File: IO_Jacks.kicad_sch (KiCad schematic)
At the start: 25 parts

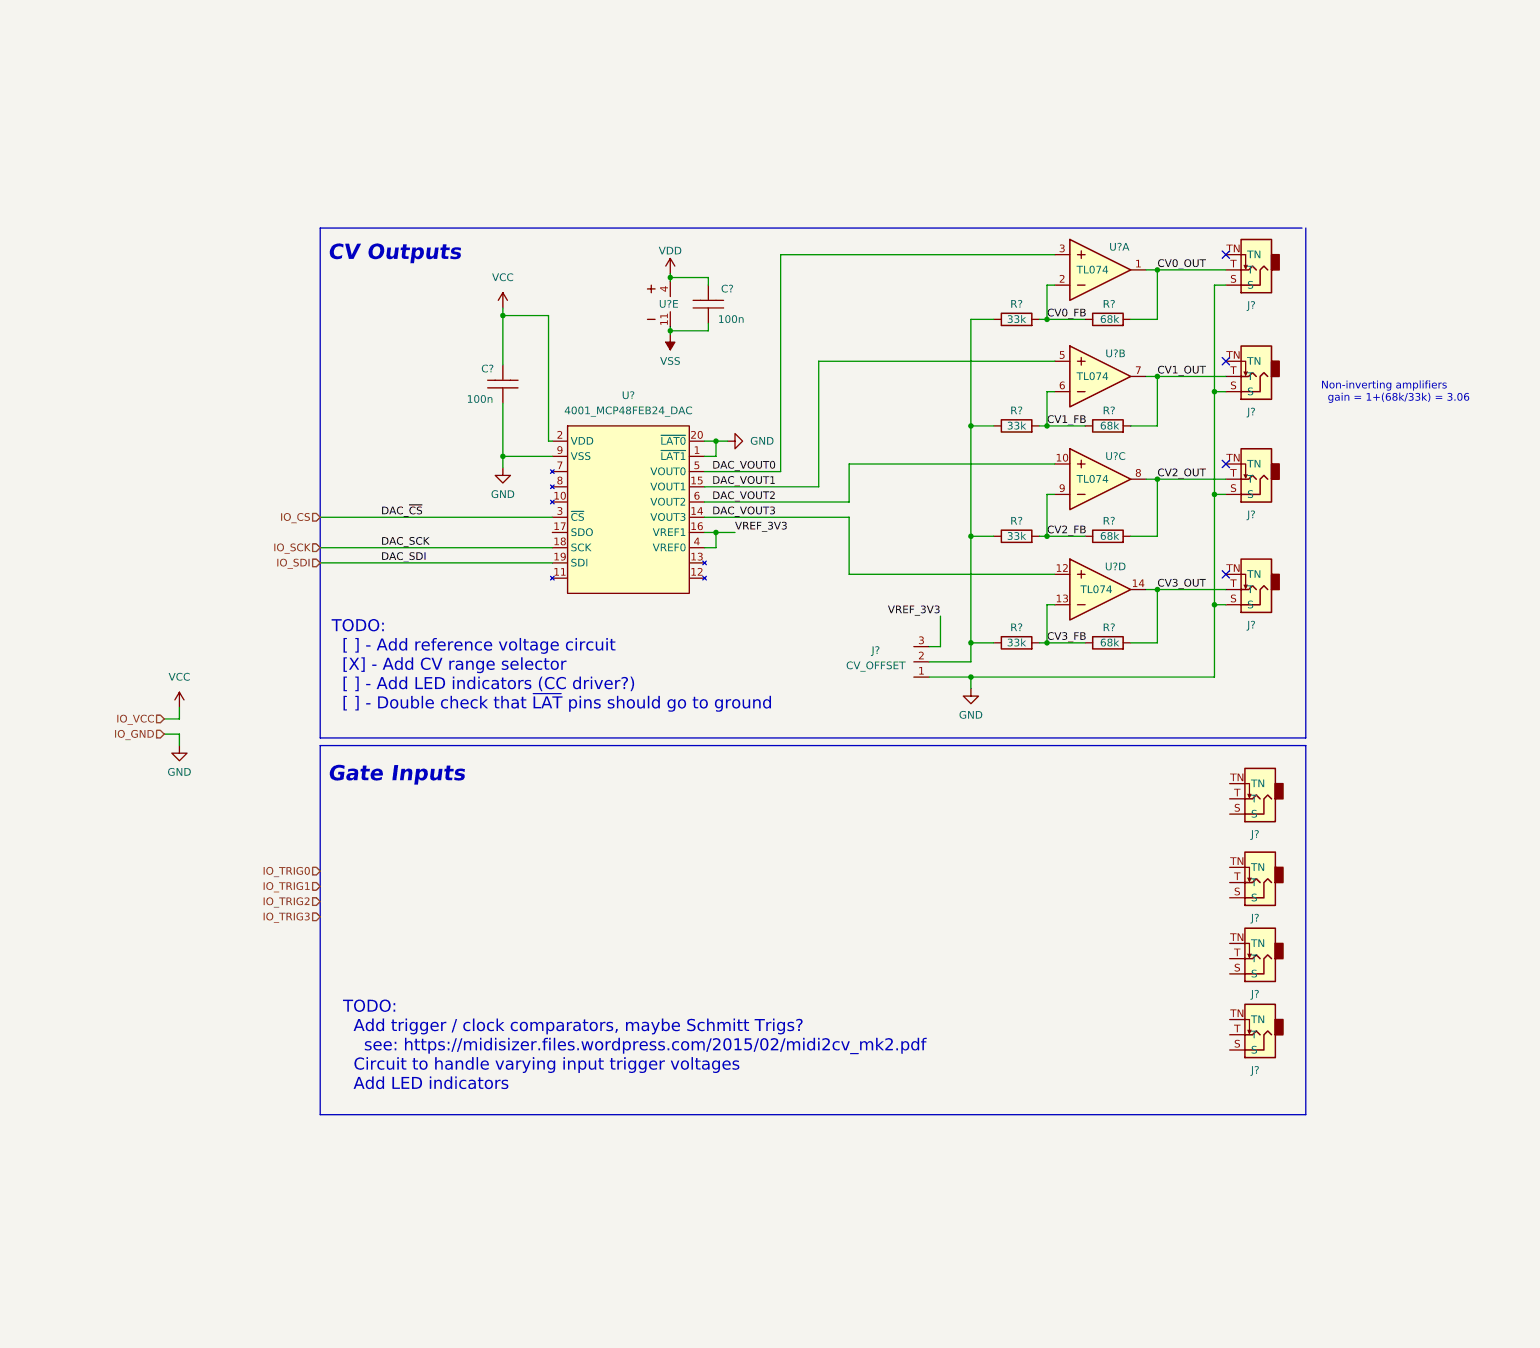
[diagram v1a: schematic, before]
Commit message: worked on gate input circuitry
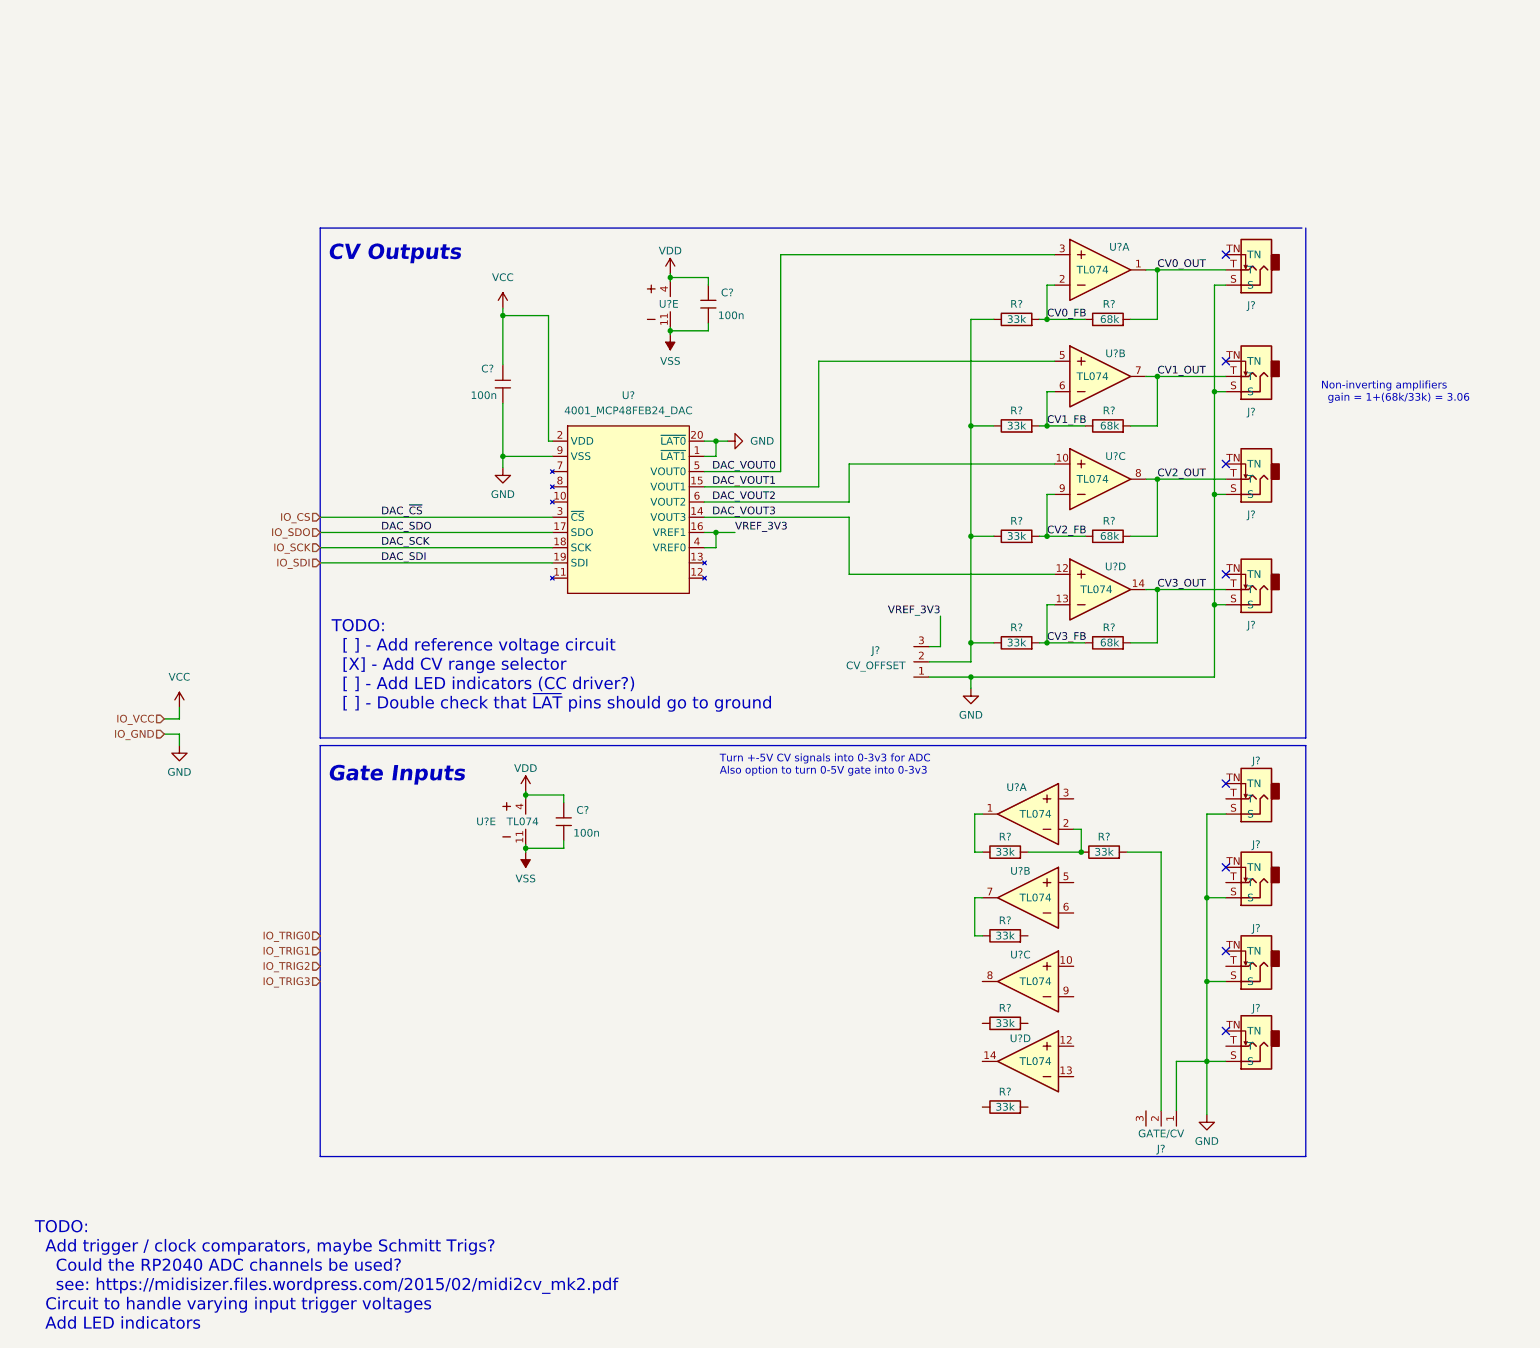
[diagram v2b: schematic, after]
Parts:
- added C?: 3089_Capacitor_100n_16V_SMD, Shulltronics_Generics:C_0402_HandSolder, symbol Shulltronics_Passives:3089_Capacitor_100n_16V_0402
- added J?: GATE/CV, Shulltronics_Connectors:3046_Header_3pos_2.54mm, symbol Shulltronics_Connectors:3046_Header_Male_Vert_3pos
- added R? (x5): 4007_Resistor_SMD_33k_0.125W_1%_1_1, Shulltronics_Passives:Resistor_0402, symbol Shulltronics_Passives:4007_Resistor_SMD_33k_0.125W_1%_1_1
- added U? (x5): 3099_TL074CPW_SMD, Shulltronics_Integrated_Circuits:3099_TL074CPW_TSSOP14, symbol Shulltronics_ICs:3099_TL074CPW_SMD
- C? (x2): symbol Shulltronics_Passives:3089_Capacitor_100n_16V_SMD -> Shulltronics_Passives:3089_Capacitor_100n_16V_0402
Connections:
- net GND: now also J?.S, J?.S, J?.S, J?.S, J?.1
- net VDD: now also C?.2, U?.4 (VCC)
- net VSS: now also C?.1, U?.11 (VEE)
- net IO_SDO: now reaches U?.17 (SDO)
- new net: R?.1, U?.1 (1OUT)
- new net: R?.1, R?.2, U?.2 (1IN-)
- new net: R?.1, U?.7 (2OUT)
- new net: J?.2, R?.2
- no-connect marks 4 -> 8
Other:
- note added: "TODO: Add trigger / clock comparators, maybe Schmitt Trigs? Could the RP2040 ADC channels be used? see: https://midisizer.files.wordpress.com/2015/02/midi2cv_mk2.pdf Circuit to handle varying input trigger voltages Add LED indicators"
- note added: "Turn +-5V CV signals into 0-3v3 for ADC Also option to turn 0-5V gate into 0-3v3"
- note removed: "TODO: Add trigger / clock comparators, maybe Schmitt Trigs? see: https://midisizer.files.wordpress.com/2015/02/midi2cv_mk2.pdf Circuit to handle varying input trigger voltages Add LED indicators"
- moved on the sheet: J?

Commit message: finished schematic (still needs double checking)
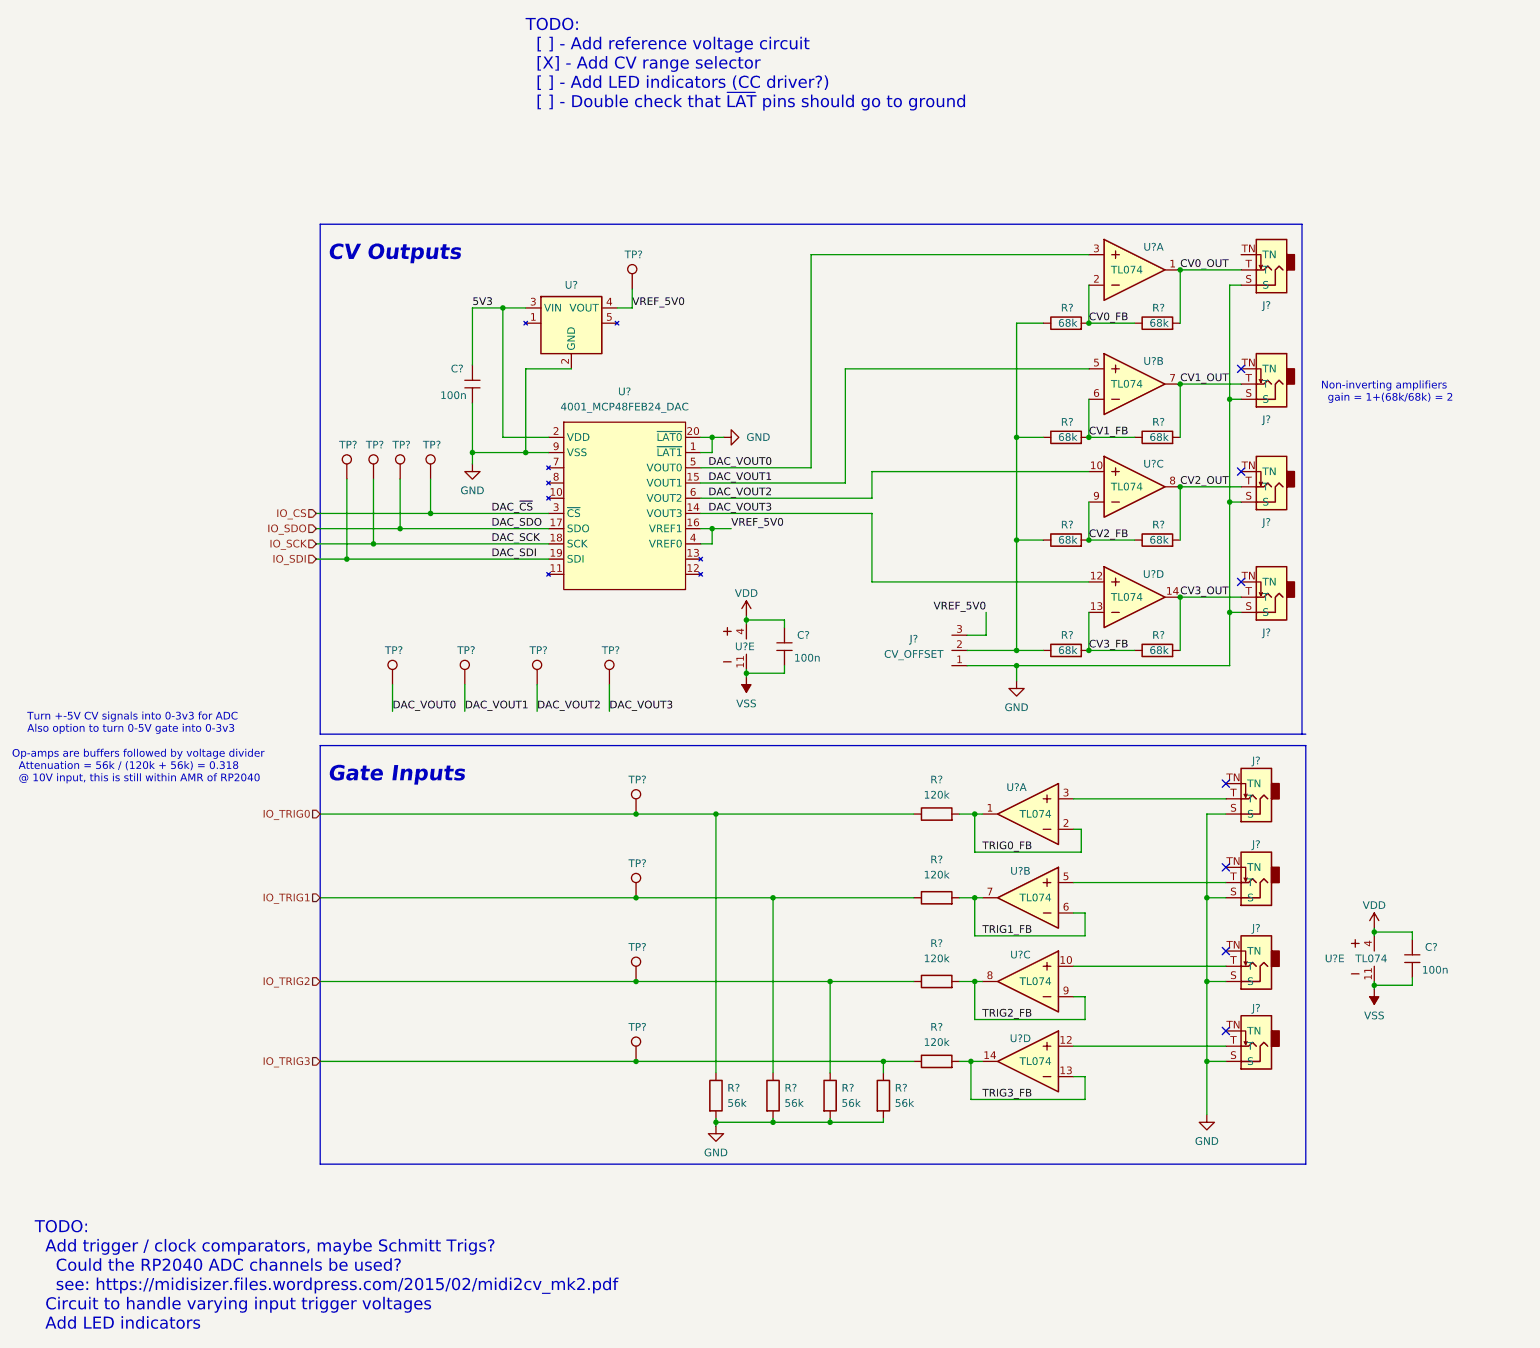
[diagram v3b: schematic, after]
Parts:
- removed J?: GATE/CV, Shulltronics_Connectors:3046_Header_3pos_2.54mm, symbol Shulltronics_Connectors:3046_Header_Male_Vert_3pos
- removed R? (x9): 4007_Resistor_SMD_33k_0.125W_1%_1_1, Shulltronics_Passives:Resistor_0402, symbol Shulltronics_Passives:4007_Resistor_SMD_33k_0.125W_1%_1_1
- removed R? (x4): 4006_Resistor_SMD_68k_0.125W_1%, Shulltronics_Passives:Resistor_0402, symbol Shulltronics_Passives:4006_Resistor_SMD_68k_0.125W_1%
- removed U? (x3): 3099_TL074CPW_SMD, Shulltronics_Integrated_Circuits:3099_TL074CPW_TSSOP14, symbol Shulltronics_ICs:3099_TL074CPW_SMD
- added R? (x4): 4022_Resistor_SMD_120k_0.125W_1%, Shulltronics_Passives:Resistor_0402, symbol Shulltronics_Passives:4022_Resistor_SMD_120k_0.125W_1%
- added R? (x4): 4023_Resistor_SMD_56k_0.125W_1%, Shulltronics_Passives:Resistor_0402, symbol Shulltronics_Passives:4023_Resistor_SMD_56k_0.125W_1%
- added R? (x8): 4006_Resistor_SMD_68k_0.125W_1%, Shulltronics_Passives:Resistor_0402, symbol Shulltronics_Passives:4006_Resistor_SMD_68k_0.125W_1%
- added TP?: DAC_SDO, Shulltronics_Generics:TestPoint_Pad_D2.0mm, symbol Shulltronics_Sch_Symbols:TestPoint
- added TP?: DAC_VOUT1, Shulltronics_Generics:TestPoint_Pad_D2.0mm, symbol Shulltronics_Sch_Symbols:TestPoint
- added TP?: DAC_SCK, Shulltronics_Generics:TestPoint_Pad_D2.0mm, symbol Shulltronics_Sch_Symbols:TestPoint
- added TP?: TRIG2, Shulltronics_Generics:TestPoint_Pad_D2.0mm, symbol Shulltronics_Sch_Symbols:TestPoint
- added TP?: TRIG1, Shulltronics_Generics:TestPoint_Pad_D2.0mm, symbol Shulltronics_Sch_Symbols:TestPoint
- added TP?: DAC_VOUT0, Shulltronics_Generics:TestPoint_Pad_D2.0mm, symbol Shulltronics_Sch_Symbols:TestPoint
- added TP?: TRIG3, Shulltronics_Generics:TestPoint_Pad_D2.0mm, symbol Shulltronics_Sch_Symbols:TestPoint
- added TP?: DAC_VOUT3, Shulltronics_Generics:TestPoint_Pad_D2.0mm, symbol Shulltronics_Sch_Symbols:TestPoint
- added TP?: DAC_SDI, Shulltronics_Generics:TestPoint_Pad_D2.0mm, symbol Shulltronics_Sch_Symbols:TestPoint
- added TP?: TRIG0, Shulltronics_Generics:TestPoint_Pad_D2.0mm, symbol Shulltronics_Sch_Symbols:TestPoint
- added TP?: DAC_VOUT2, Shulltronics_Generics:TestPoint_Pad_D2.0mm, symbol Shulltronics_Sch_Symbols:TestPoint
- added TP?: DAC_~{CS}, Shulltronics_Generics:TestPoint_Pad_D2.0mm, symbol Shulltronics_Sch_Symbols:TestPoint
- added TP?: VREF_5V0, Shulltronics_Generics:TestPoint_Pad_D2.0mm, symbol Shulltronics_Sch_Symbols:TestPoint
- added U? (x3): 3099_TL074CPW_SMD, Shulltronics_Integrated_Circuits:3099_TL074CPW_TSSOP14, symbol Shulltronics_ICs:3099_TL074CPW_SMD
- added U?: 4014_Voltage_Reference_5V_SOT23-6, Shulltronics_Generics:SOT-23-5, symbol Shulltronics_Semiconductors:4014_Voltage_Reference_5V_SOT23-6
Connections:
- net CV0_FB: now also R?.1, R?.2
- net CV0_OUT: now also R?.2
- net CV1_FB: now also R?.1, R?.2, U?.6 (2IN-)
- net CV1_OUT: now also R?.2, U?.7 (2OUT)
- net CV2_FB: now also R?.1, R?.2, U?.9 (3IN-)
- net CV2_OUT: now also R?.2, U?.8 (3OUT)
- net CV3_FB: now also R?.1, R?.2, U?.13 (4IN-)
- net CV3_OUT: now also R?.2, U?.14 (4OUT)
- net DAC_VOUT0: now also TP?.1
- net DAC_VOUT1: now also TP?.1, U?.5 (2IN+)
- net DAC_VOUT2: now also TP?.1, U?.10 (3IN+)
- net DAC_VOUT3: now also TP?.1, U?.12 (4IN+)
- net GND: now also R?.2, R?.2, R?.2, R?.2, U?.2 (GND)
- net IO_CS: now also TP?.1
- net IO_SCK: now also TP?.1
- net IO_SDI: now also TP?.1
- net IO_SDO: now also TP?.1
- net IO_TRIG0: now also R?.1, R?.1, TP?.1
- net IO_TRIG1: now also R?.1, R?.1, TP?.1
- net IO_TRIG2: now also R?.1, R?.1, TP?.1
- net IO_TRIG3: now also R?.1, R?.1, TP?.1
- net TRIG0_FB: now reaches U?.1 (1OUT)
- net TRIG0_FB: now also U?.2 (1IN-), R?.2
- net at J?.T: now also U?.10 (3IN+)
- net TRIG2_FB: now reaches U?.8 (3OUT)
- net TRIG2_FB: now also U?.9 (3IN-), R?.2
- net at U?.5 (2IN+): now also J?.T
- net TRIG1_FB: now reaches U?.6 (2IN-)
- net TRIG1_FB: now also U?.7 (2OUT), R?.2
- net at J?.T: now also U?.3 (1IN+)
- net at J?.2: now also R?.1, R?.1, R?.1, R?.1
- net at U?.12 (4IN+): now also J?.T
- net TRIG3_FB: now reaches U?.13 (4IN-)
- net TRIG3_FB: now also U?.14 (4OUT), R?.2
- net VCC renamed 5V3
- net 5V3: now also U?.3 (VIN)
- net VREF_3V3 renamed VREF_5V0
- net VREF_5V0: now also TP?.1, U?.4 (VOUT)
- no-connect marks 8 -> 7
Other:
- note added: "Non-inverting amplifiers gain = 1+(68k/68k) = 2"
- note added: "Op-amps are buffers followed by voltage divider Attenuation = 56k / (120k + 56k) = 0.318 @ 10V input, this is still within AMR of RP2040"
- note removed: "Non-inverting amplifiers gain = 1+(68k/33k) = 3.06"
- moved on the sheet: C?, J?, U?, U?A, U?E
